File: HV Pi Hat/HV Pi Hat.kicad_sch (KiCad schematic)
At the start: 16 parts, among them J3 SHV-R, J4 SHV-R

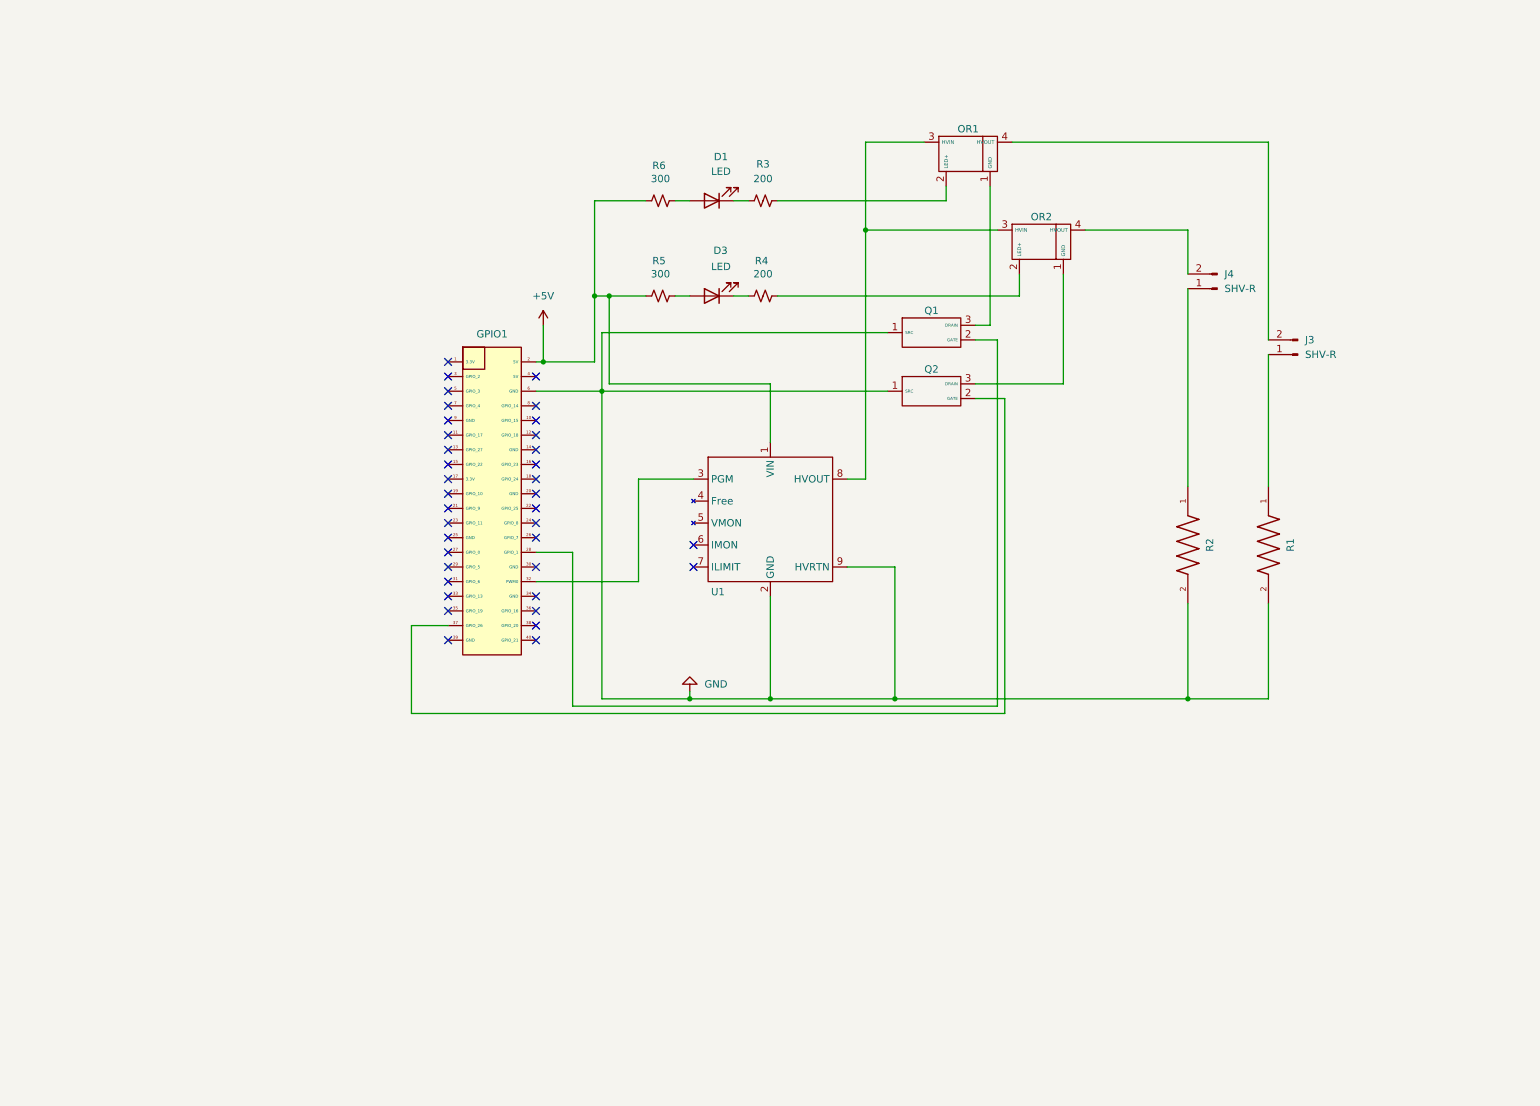
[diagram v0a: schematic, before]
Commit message: Foundation, HV design review, and cross-agent handoff docs
Self-contained libraries (HV_Pi_Hat.pretty + HV_Electronics/MHR0317 symbols) with relinked lib tables; HV spacing enforced via 'HV Pi Hat.kicad_dru' (4mm clearance/creepage/edge on HV nets); R1/R2 bleeders corrected to 100M; datasheets/ added + index; design review (REVIEW_FINDINGS) + corrected active charge/discharge design (CONTROL_DESIGN); schematic control rework started (op-amp PGM stage, ILIMIT tie, decoupling); docs reorganized under docs/ with a short CLAUDE.md index; stop tracking regenerable render/drc artifacts; ignore editor/backup cruft.

Co-Authored-By: Claude Opus 4.8 (1M context) <noreply@anthropic.com>
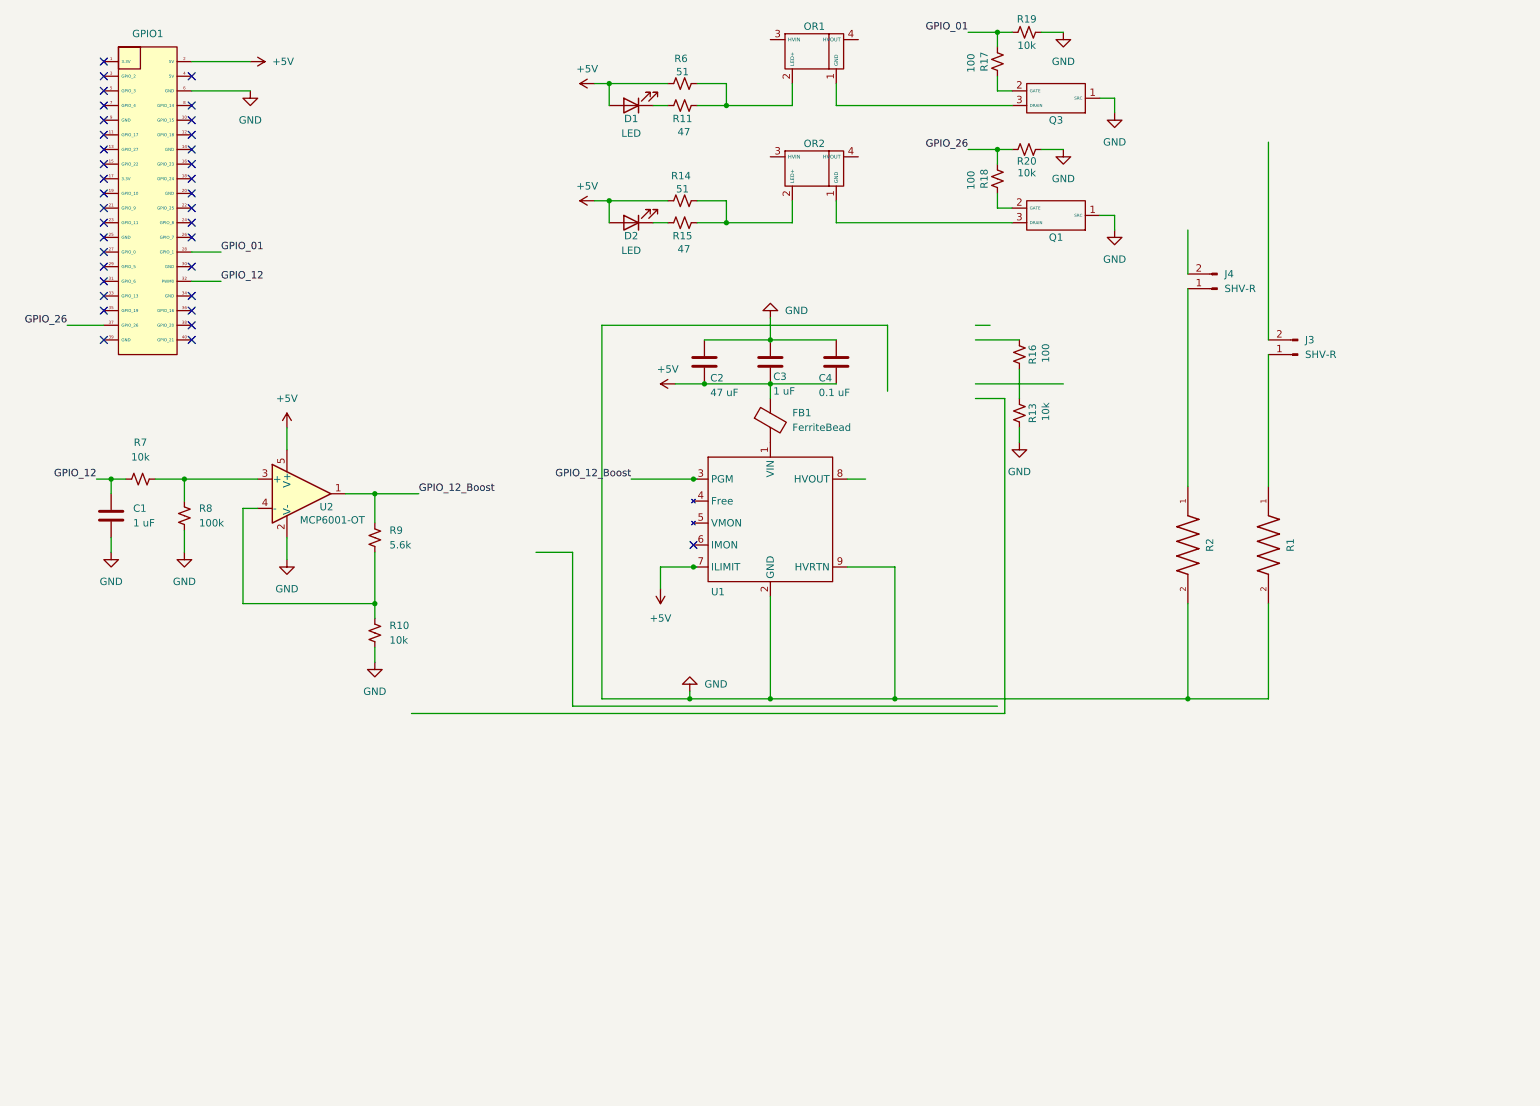
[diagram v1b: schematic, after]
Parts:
- removed D3: LED, 3372-BND0603JKRS001TR-ND:Untitled, symbol Device:LED
- removed Q2: ~, TN0610N3_G_P013_Footprint:TO-92_MC_MCH, symbol HV_Electronics:TN0610N3_G_P013
- removed R3, R4: 200, 3372-BND0603JKRS001TR-ND:Resistor 200 O, symbol Device:R_Small_US
- removed R5: 300, 3372-CR0402FC300RS1TR-ND:Resistor 300 O, symbol Device:R_Small_US
- added C1, C3: 1 uF, symbol Device:C
- added C2: 47 uF, symbol Device:C
- added C4: 0.1 uF, symbol Device:C
- added D2: LED, 3372-BND0603JKRS001TR-ND:Untitled, symbol Device:LED
- added FB1: FerriteBead, symbol Device:FerriteBead
- added Q3: (no value), TN0610N3_G_P013_Footprint:TO-92_MC_MCH, symbol HV_Electronics:TN0610N3_G_P013
- added R10, R7: 10k, symbol Device:R_Small_US
- added R11, R15: 47, 3372-CR0402FC300RS1TR-ND:Resistor 300 O, symbol Device:R_Small_US
- added R13, R19, R20: 10k, 3372-CR0402FC300RS1TR-ND:Resistor 300 O, symbol Device:R_Small_US
- added R14: 51, 3372-CR0402FC300RS1TR-ND:Resistor 300 O, symbol Device:R_Small_US
- added R16, R17, R18: 100, 3372-CR0402FC300RS1TR-ND:Resistor 300 O, symbol Device:R_Small_US
- added R8: 100k, symbol Device:R_Small_US
- added R9: 5.6k, symbol Device:R_Small_US
- added U2: MCP6001-OT, Package_TO_SOT_SMD:SOT-23-5, symbol Amplifier_Operational:MCP6001-OT
- GPIO1, OR1, OR2, Q1, U1: value ~ -> (none)
- R6: value 300 -> 51
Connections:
- net +5V: now also D1.2 (A), U1.7 (ILIMIT), C2.2, C3.2, C4.2, D2.2 (A), FB1.1, R14.1, U2.5 (V+); no longer U1.1 (VIN)
- net GND: now also C1.2, C2.1, C3.1, C4.1, Q3.1 (SRC), R10.1, R13.1, R19.1, R20.1, R8.1, U2.2 (V-)
- net at J3.2 (Pin_2): no longer names the net of J3.2 (Pin_2)
- net at J3.2 (Pin_2): no longer OR1.4 (HVOUT)
- net GPIO_26: now reaches GPIO1.37 (GPIO_26)
- net GPIO_26: now also R18.1, R20.2
- net at OR2.1 (GND): now also Q1.3 (DRAIN)
- net at D1.1 (K): now also R11.1
- net at OR1.2 (LED+): now also R6.2, R11.2
- net at OR1.1 (GND): now also Q3.3 (DRAIN); no longer Q1.3 (DRAIN)
- net at Q1.2 (GATE): now also R18.2; no longer GPIO1.28 (GPIO_1)
- net GPIO_12: now reaches GPIO1.32 (GPIO_12)
- net GPIO_12: now also C1.1, R7.1; no longer U1.3 (PGM)
- net at OR2.2 (LED+): now also R14.2, R15.2
- net at OR2.4 (HVOUT): no longer J4.2 (Pin_2)
- new net: R7.2, R8.2, U2.3 (+)
- new net: R10.2, R9.1, U2.4 (-)
- new net: R13.2, R16.1
- new net: D2.1 (K), R15.1
- new net: Q3.2 (GATE), R17.2
- new net: FB1.2, U1.1 (VIN)
- new net GPIO_01: GPIO1.28 (GPIO_1), R17.1, R19.2
- new net GPIO_12_Boost: R9.2, U1.3 (PGM), U2.1
- now unconnected: OR1.3 (HVIN), OR2.3 (HVIN), U1.8 (HVOUT)
- no-connect marks 37 -> 36
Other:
- moved on the sheet: D1, GPIO1, OR1, OR2, R6

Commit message: Decision A1: HV Pi Hat autonomous build + HV/LV route pass
Schematic finalized to match CONTROL_DESIGN (netlist 30/30, ERC 0); PCB regenerated, placed, HV/LV lane-separated; HV routed on outer layers with inner-layer voids + GND guard pours; custom JLCPCB thick stackup + conformal-coat creepage (kicad_dru 2 mm air / 4 mm pour); sourced BOM; preliminary gerbers under fab/preliminary_DO_NOT_FAB; docs AUTONOMOUS_BUILD_LOG/BOM_SOURCED/HV_CONNECTOR_OPTIONS + updated STATUS/DECISIONS/EESCHEMA_TODO; toolchain now KiCad 10. Pending mandatory human-EE review before fab/energizing (5 kV).

Co-Authored-By: Claude Opus 4.8 (1M context) <noreply@anthropic.com>
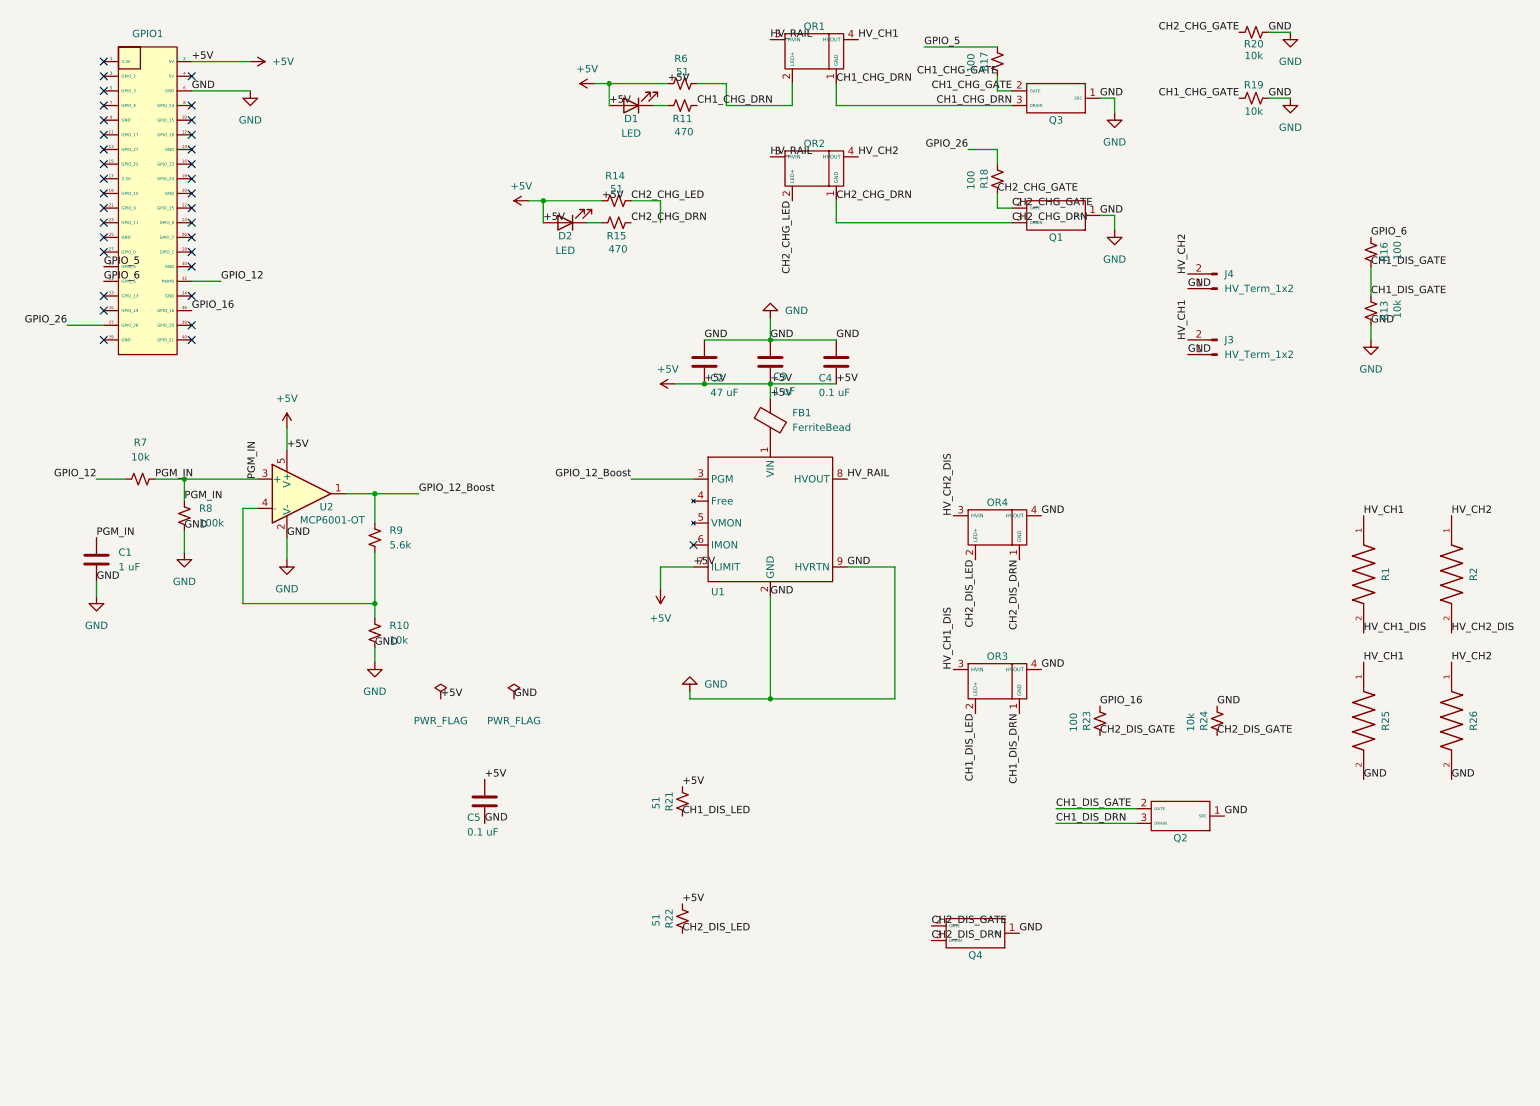
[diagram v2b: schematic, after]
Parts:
- added C5: 0.1 uF, Capacitor_SMD:C_0603_1608Metric, symbol Device:C
- added OR3, OR4: (no value), HV_Footprints:HVM OR-100, symbol HV_Electronics:HVM_OR-100
- added Q2, Q4: (no value), TN0610N3_G_P013_Footprint:TO-92_MC_MCH, symbol HV_Electronics:TN0610N3_G_P013
- added R21, R22: 51, Resistor_SMD:R_0603_1608Metric, symbol Device:R_Small_US
- added R23: 100, Resistor_SMD:R_0603_1608Metric, symbol Device:R_Small_US
- added R24: 10k, Resistor_SMD:R_0603_1608Metric, symbol Device:R_Small_US
- added R25, R26: 1G, MHR0317SA107F70:RESRR1524W50L1760T250H500, symbol MHR0317SA107F70:MHR0317SA107F70
- C1, C3, C4: footprint (none) -> Capacitor_SMD:C_0603_1608Metric
- C2: footprint (none) -> Capacitor_SMD:C_1206_3216Metric
- D1, D2: footprint 3372-BND0603JKRS001TR-ND:Untitled -> LED_SMD:LED_0603_1608Metric
- FB1: footprint (none) -> Inductor_SMD:L_0805_2012Metric
- J3, J4: value SHV-R -> HV_Term_1x2; footprint 4912-SHV-R-ND:4912-SHV-R-ND -> TerminalBlock_RND:TerminalBlock_RND_205-00241_1x02_P10.16mm_Horizontal
- R10, R7, R8, R9: footprint (none) -> Resistor_SMD:R_0603_1608Metric
- R11, R15: value 47 -> 470; footprint 3372-CR0402FC300RS1TR-ND:Resistor 300 O -> Resistor_SMD:R_0603_1608Metric
- R13, R14, R16, R17, R18, R19, R20, R6: footprint 3372-CR0402FC300RS1TR-ND:Resistor 300 O -> Resistor_SMD:R_0603_1608Metric
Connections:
- net +5V: now also C5.1, R21.1, R22.1
- net GND: now also J3.1 (Pin_1), J4.1 (Pin_1), C5.2, OR3.4 (HVOUT), OR4.4 (HVOUT), Q2.1 (SRC), Q4.1 (SRC), R24.1, R25.2, R26.2; no longer R1.2, R2.2
- net GPIO_12: no longer C1.1
- net GPIO_26: no longer R20.2
- net PGM_IN: now reaches R7.2, R8.2, U2.3 (+)
- net PGM_IN: now also C1.1
- net HV_CH1: now reaches R1.1
- net HV_CH1: now also J3.2 (Pin_2), OR1.4 (HVOUT), R25.1; no longer J3.1 (Pin_1)
- net HV_CH2: now reaches R2.1
- net HV_CH2: now also J4.2 (Pin_2), OR2.4 (HVOUT), R26.1; no longer J4.1 (Pin_1)
- net CH1_DIS_GATE: now reaches R13.2, R16.1
- net CH1_DIS_GATE: now also Q2.2 (GATE)
- net CH1_CHG_DRN: now reaches OR1.1 (GND), Q3.3 (DRAIN)
- net CH1_CHG_DRN: now also R11.2
- net at OR1.2 (LED+), R6.2: no longer R11.2
- net HV_RAIL: now reaches OR1.3 (HVIN)
- net HV_RAIL: now also OR2.3 (HVIN), U1.8 (HVOUT)
- net CH2_CHG_LED: now reaches OR2.2 (LED+), R14.2
- net CH2_CHG_LED: no longer R15.2
- net GPIO_5: now reaches GPIO1.29 (GPIO_5)
- net GPIO_5: now also R17.1
- net GPIO_6: now reaches GPIO1.31 (GPIO_6)
- net GPIO_6: now also R16.2
- net GPIO_16: now reaches GPIO1.36 (GPIO_16)
- net GPIO_16: now also R23.1
- net CH1_CHG_GATE: now reaches Q3.2 (GATE), R17.2
- net CH1_CHG_GATE: now also R19.2
- net CH2_CHG_GATE: now reaches Q1.2 (GATE), R18.2
- net CH2_CHG_GATE: now also R20.2
- net CH2_CHG_DRN: now reaches OR2.1 (GND), Q1.3 (DRAIN)
- net CH2_CHG_DRN: now also R15.2
- removed net GPIO_01: GPIO1.28 (GPIO_1), R17.1, R19.2
- new net CH1_DIS_DRN: OR3.1 (GND), Q2.3 (DRAIN)
- new net CH1_DIS_LED: OR3.2 (LED+), R21.2
- new net CH2_DIS_DRN: OR4.1 (GND), Q4.3 (DRAIN)
- new net CH2_DIS_GATE: Q4.2 (GATE), R23.2, R24.2
- new net CH2_DIS_LED: OR4.2 (LED+), R22.2
- new net HV_CH1_DIS: OR3.3 (HVIN), R1.2
- new net HV_CH2_DIS: OR4.3 (HVIN), R2.2
- no-connect marks 36 -> 34
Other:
- moved on the sheet: C1, D2, J3, R1, R13, R14, R15, R16, R19, R2, R20

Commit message: Rev B: HAT+ outline board with soldered HV leads and a potted HV zone
Issue #6. Promotes the placement study (#4) to the main board:

- Schematic: J3/J4 footprint -> HV_Footprints:HV_LeadPair_P6.00mm
  (pad 1 return, pad 2 HV, 6.0 mm pitch). Netlist connectivity checked
  identical before/after (66 nets, 146 pins); ERC 0 errors.
- New footprint generated by tools/MakeLeadPair.py.
- Board: 65 x 56.5 mm HAT+ outline, study placement with J3 at the right
  edge and J4 along the bottom, pot outline + inner voids, routed by
  tools/revb/AutoRoute.py with LV kept out of the pot except over U1's
  LV pin row, GND pours on F/B.
- DRC: 0 unconnected, 0 clearance/creepage/edge errors at the 2 mm
  interim rule; schematic parity only the pre-existing D1/D2 Sim.Pins
  and H1-H4 items. Pot margin 3.00 mm. Through-board minimum 2.23 mm.
- tools/HvInterlayer.py now uses true radii for round pads.
- Docs: OPTO-100 package size corrected from the datasheet (0.40 x 0.24
  x 0.25 in), J3/J4 BOM rows, BOM.csv, CLAUDE/TOOLING/README, ADR-0004
  status, rev B renders.

Pi 5 underside keepouts are not in this commit.

Co-Authored-By: Claude Opus 5.5 <noreply@anthropic.com>
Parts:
- J3, J4: value HV_Term_1x2 -> HV_LeadPair; footprint TerminalBlock_RND:TerminalBlock_RND_205-00241_1x02_P10.16mm_Horizontal -> HV_Footprints:HV_LeadPair_P6.00mm
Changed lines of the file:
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@@
 			)
 		)
-		(property "Value" "HV_Term_1x2"
+		(property "Value" "HV_LeadPair"
 			(at 223.52 72.3899 0)
 			(show_name no)
@@
 			)
 		)
-		(property "Footprint" "TerminalBlock_RND:TerminalBlock_RND_205-00241_1x02_P10.16mm_Horizontal"
+		(property "Footprint" "HV_Footprints:HV_LeadPair_P6.00mm"
 			(at 222.25 72.39 0)
 			(hide yes)
@@
 			)
 		)
-		(property "Description" "Generic connector, single row, 01x02, script generated"
+		(property "Description" "Soldered HV lead pair for the potted zone: pin 1 return (GND), pin 2 HV (ADR-0003)"
 			(at 222.25 72.39 0)
 			(hide yes)
@@
 			)
 		)
-		(property "Value" "HV_Term_1x2"
+		(property "Value" "HV_LeadPair"
 			(at 223.52 60.9599 0)
 			(show_name no)
@@
 			)
 		)
-		(property "Footprint" "TerminalBlock_RND:TerminalBlock_RND_205-00241_1x02_P10.16mm_Horizontal"
+		(property "Footprint" "HV_Footprints:HV_LeadPair_P6.00mm"
 			(at 222.25 60.96 0)
 			(hide yes)
@@
 			)
 		)
-		(property "Description" "Generic connector, single row, 01x02, script generated"
+		(property "Description" "Soldered HV lead pair for the potted zone: pin 1 return (GND), pin 2 HV (ADR-0003)"
 			(at 222.25 60.96 0)
 			(hide yes)

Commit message: Rev B: opto drive, ID EEPROM, underside socket, NPTH holes, bench plan
Implements the recommendations from the 2026-10-08 decision list:

- ADR-0006: opto LED resistors R6/R14/R21/R22 51 Ohm 0603 -> 15 Ohm
  1206. The OPTO-100 datasheet's CTR graph starts at about 40 mA of
  LED current; 51 Ohm gave about 38 mA. 15 Ohm gives about 110 mA.
- ADR-0007: HAT+ ID EEPROM (CAT24C32 at 0x50, 3.9k ID pull-ups, 1k WP
  pull-up + TP1, 100 nF) added to the schematic by
  tools/revb/AddIdEeprom.py; netlist checked: only the four new nets
  (+3V3, ID_SD, ID_SC, ID_WP) and GND gained pins, everything else
  identical. GPIO1 becomes a bottom-side 2x20 socket (pads verified
  identical); H1-H4 become unplated 2.75 mm holes.
- tools/revb/BuildRevB.py now syncs the board from the schematic
  netlist (footprint swaps, new parts, every pad net).
- docs/BENCH_TESTS.md: T1-T9, including an opto HV lead polarity check
  (a reversed photodiode conducts with no light).
- Docs: CONTROL_DESIGN, CLAUDE, datasheets README correction, BOM.

ERC 0 errors (8 warnings, 7 pre-existing). DRC 0 unconnected, 0
electrical; parity 6 pre-existing (D1/D2 Sim.Pins, H1-H4). Pot margin
3.00 mm, through-board 2.23 mm, Active Cooler room 3.3 mm at 20 mm.

Co-Authored-By: Claude Opus 5.5 <noreply@anthropic.com>
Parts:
- added C6: 0.1 uF, Capacitor_SMD:C_0603_1608Metric, symbol Device:C
- added R27, R28: 3.9k, Resistor_SMD:R_0603_1608Metric, symbol Device:R_Small_US
- added R29: 1k, Resistor_SMD:R_0603_1608Metric, symbol Device:R_Small_US
- added TP1: ID_WP, TestPoint:TestPoint_Pad_D1.5mm, symbol Connector:TestPoint
- added U3: CAT24C32, Package_SO:SOIC-8_3.9x4.9mm_P1.27mm, symbol Memory_EEPROM:24LC16
- GPIO1: value (none) -> Samtec ESQ-120-14-G-D; footprint Connector_PinHeader_2.54mm:PinHeader_2x20_P2.54mm_Vertical -> Connector_PinSocket_2.54mm:PinSocket_2x20_P2.54mm_Vertical
- R14, R21, R22, R6: value 51 -> 15; footprint Resistor_SMD:R_0603_1608Metric -> Resistor_SMD:R_1206_3216Metric
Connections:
- net GND: now also C6.2, U3.1 (A0), U3.2 (A1), U3.3 (A2), U3.4 (GND)
- net +3V3: now reaches GPIO1.1 (3.3V)
- net +3V3: now also C6.1, R27.1, R28.1, R29.1, U3.8 (VCC)
- net ID_SD: now reaches GPIO1.27 (GPIO_0)
- net ID_SD: now also R27.2, U3.5 (SDA)
- net ID_SC: now reaches GPIO1.28 (GPIO_1)
- net ID_SC: now also R28.2, U3.6 (SCL)
- new net ID_WP: R29.2, TP1.1, U3.7 (WP)
- no-connect marks 34 -> 31
